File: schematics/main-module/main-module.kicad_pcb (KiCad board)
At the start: 4 copper layers, 134 x 52 mm, 101 parts, among them J1 Conn_01x02_Socket, J2 USB_C_Receptacle_USB2.0, J3 Charger, J4 Power, J5 Limit Switch, J6 Conn_01x04_Socket, Q1 IRLML0030, Q2 IRF7425PbF, Q3 BC847, Q4 BC847, Q6 IRLML0030, Q7 IRF7832PbF, Q8 IRF7832PbF, SW1 KLS7-TS3601-5.0-180, SW2 KLS7-TS3601-5.0-180, T1 Transformer_1P_SS, U1 CP2102N-Axx-xQFN28, U10 SRX882@315Mhz, U11 FAN3100, U12 FAN3100, U13 TMC2209_Module, U3 AMS1117-5.0, U4 AMS1117-3.3, U6 SRX882@433Mhz, U7 STX882@433Mhz, U8 ESP32-WROOM-32, U9 TL494

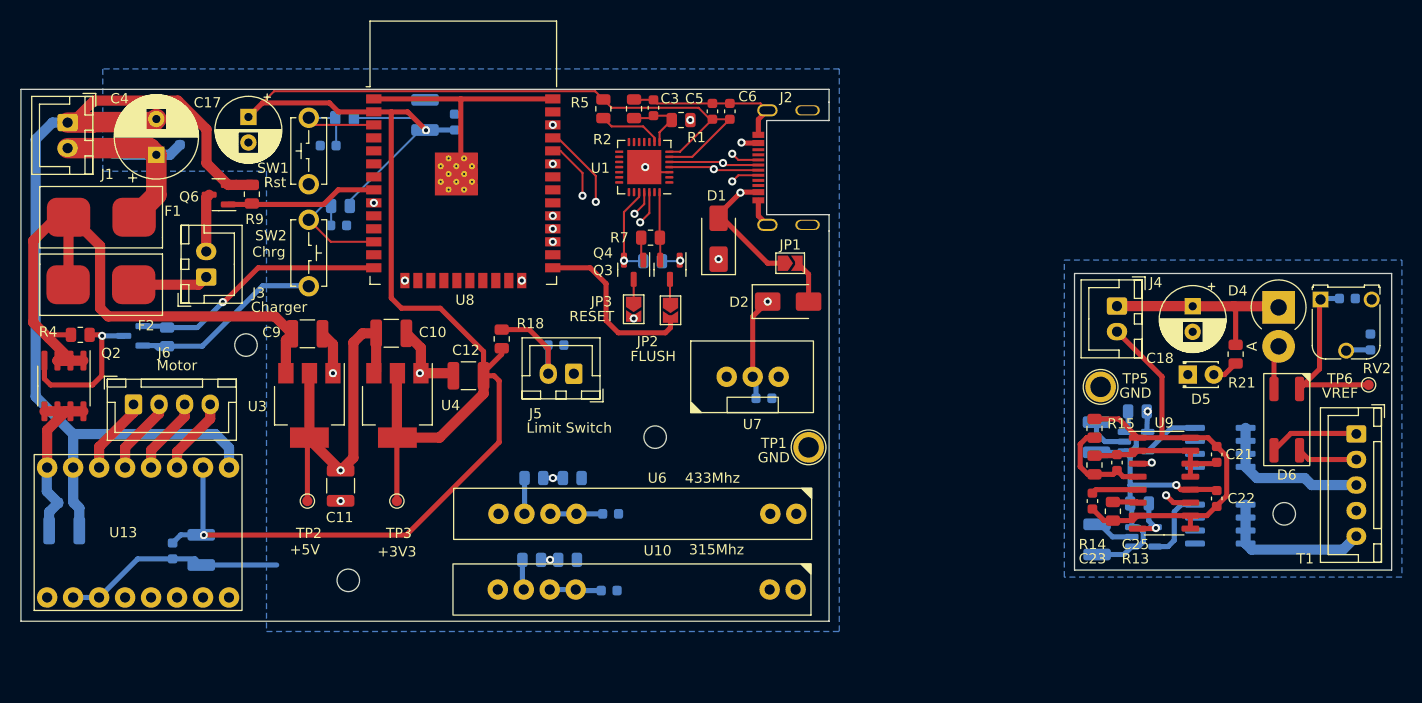
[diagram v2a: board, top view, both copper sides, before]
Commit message: 1. board: added protection against high noise in case of endstop is broken. 2. board: added step-up 7.5V -> 15V for charger. 3. firmware - added support for noise protection and some changes in stepper logic
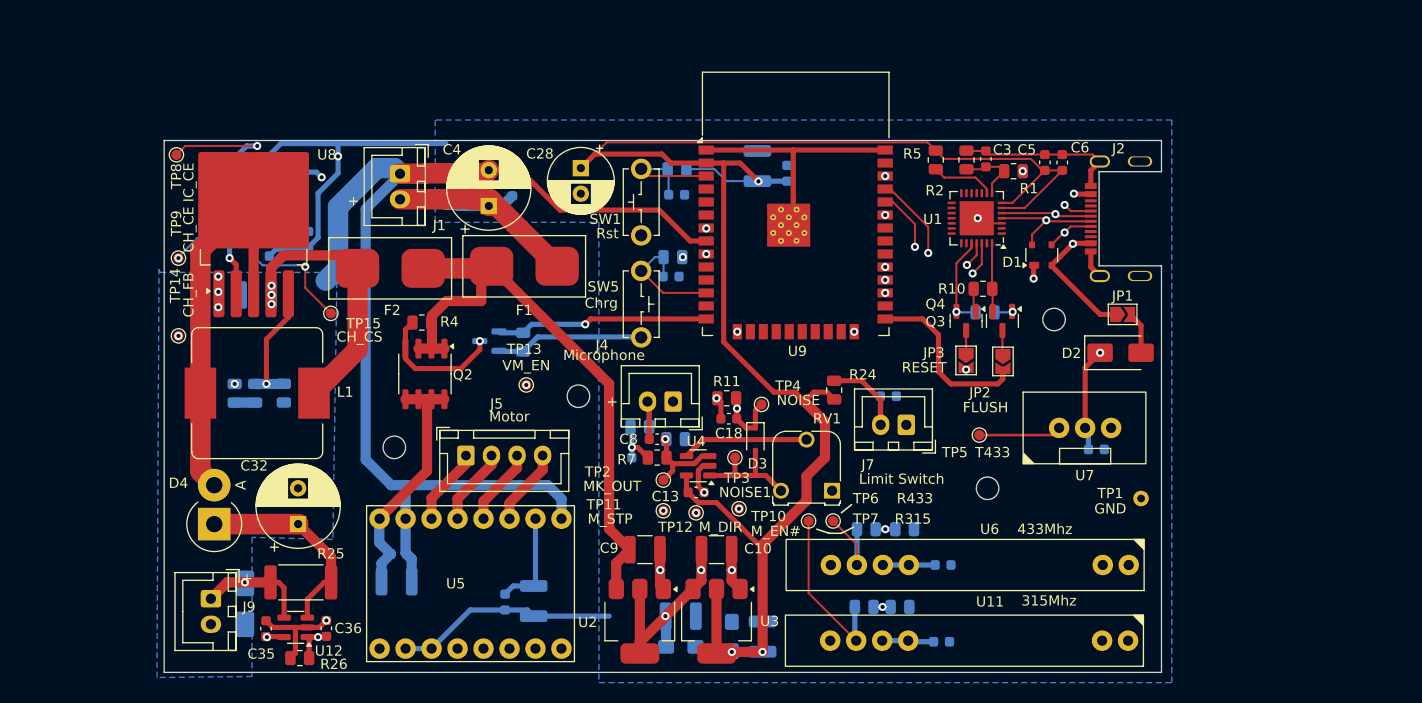
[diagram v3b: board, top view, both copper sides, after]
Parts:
- removed the C21 at (158.9, 77.7)
- removed the C22 at (158.9, 82.0)
- removed the C23 at (146.8, 82.2)
- removed the C28 at (147.2, 76.0)
- removed the C30 at (147.2, 86.0)
- removed the H3 at (74.0, 90.0)
- removed J3: Charger, Connector_JST:JST_XH_B2B-XH-A_1x02_P2.50mm_Vertical
- removed Q6: IRLML0030, Package_TO_SOT_SMD:SOT-23
- removed Q7, Q8: IRF7832PbF, Package_SO:SOIC-8_3.9x4.9mm_P1.27mm
- removed the R13 at (148.8, 83.2)
- removed the R14 at (146.9, 78.7)
- removed the R9 at (64.6, 52.2)
- removed RV2: 1K, Potentiometer_THT:Potentiometer_Runtron_RM-065_Vertical
- removed T1: Transformer_1P_SS, Connector_JST:JST_XH_B5B-XH-A_1x05_P2.50mm_Vertical
- removed the U11 at (151.7, 85.8)
- removed the U9 at (153.8, 80.5)
- added C13: 100 nF, Capacitor_SMD:C_0603_1608Metric, F.Cu at (108.0, 81.4)
- added C16: 22 uF, Capacitor_Tantalum_SMD:CP_EIA-3216-10_Kemet-I_Pad1.58x1.35mm_HandSolder, B.Cu at (106.5, 96.5)
- added C17: 22 uF, Capacitor_Tantalum_SMD:CP_EIA-3216-10_Kemet-I_Pad1.58x1.35mm_HandSolder, B.Cu at (111.5, 95.5)
- added C24: 22 uF, Capacitor_SMD:C_1210_3225Metric, B.Cu at (65.0, 62.1)
- added C26: 10 nF, Capacitor_SMD:C_0603_1608Metric, B.Cu at (70.1, 56.7)
- added C29: 100 nF, Capacitor_SMD:C_0603_1608Metric, B.Cu at (65.4, 50.1)
- added C32: 220 uF@35V, Capacitor_THT:CP_Radial_D8.0mm_P3.50mm, F.Cu at (69.1, 84.5)
- added C36: 10 nF, Capacitor_SMD:C_0603_1608Metric, F.Cu at (71.9, 94.7)
- added C7: 100 nF, Capacitor_SMD:C_0603_1608Metric, B.Cu at (102.5, 78.0)
- added C8: 47 nF, Capacitor_SMD:C_0603_1608Metric, F.Cu at (104.2, 76.2)
- added D3: BAV21WS, Diode_SMD:D_SOD-323F, F.Cu at (113.8, 76.2)
- added H4: MountingHole, MountingHole:MountingHole_2.2mm_M2, F.Cu at (143.0, 64.5)
- added J9: Charger port, Connector_JST:JST_XH_B2B-XH-A_1x02_P2.50mm_Vertical, F.Cu at (60.6, 91.8)
- added L1: AMPLF1260, 4.7 uH, Inductor_SMD:L_TaiTech_TMPC1265_13.5x12.5mm, F.Cu at (65.1, 71.7)
- added R11: 10K, Resistor_SMD:R_0805_2012Metric, F.Cu at (111.0, 72.2)
- added R18: 200K, Resistor_SMD:R_0805_2012Metric, B.Cu at (60.2, 55.6)
- added R19: 1K, Resistor_SMD:R_0805_2012Metric, B.Cu at (62.9, 71.7)
- added R20: 10K, Resistor_SMD:R_0805_2012Metric, B.Cu at (64.9, 71.7)
- added R25: 0,5, Resistor_SMD:R_2512_6332Metric, F.Cu at (69.4, 90.2)
- added R26: 100K, Resistor_SMD:R_0805_2012Metric, F.Cu at (69.3, 97.6)
- added R6: 10K, Resistor_SMD:R_0805_2012Metric, B.Cu at (102.5, 75.0)
- added R7: 20K, Resistor_SMD:R_0805_2012Metric, F.Cu at (104.2, 78.0)
- added R8: 10K, Resistor_SMD:R_0805_2012Metric, B.Cu at (106.0, 76.2)
- added RV1: RM065, 100K, Potentiometer_THT:Potentiometer_Runtron_RM-065_Vertical, F.Cu at (121.3, 81.2)
- added TP10: M_EN#, TestPoint:TestPoint_Pad_D1.0mm, F.Cu at (112.2, 83.0)
- added TP11: M_STP, TestPoint:TestPoint_Pad_D1.0mm, F.Cu at (104.8, 83.2)
- added TP12: M_DIR, TestPoint:TestPoint_Pad_D1.0mm, F.Cu at (108.0, 83.4)
- added TP13: VM_EN, TestPoint:TestPoint_Pad_D1.0mm, F.Cu at (91.4, 70.9)
- added TP14: CH_FB, TestPoint:TestPoint_Pad_D1.0mm, F.Cu at (57.4, 66.1)
- added TP15: CH_CS, TestPoint:TestPoint_Pad_D1.0mm, F.Cu at (72.3, 63.9)
- added TP4: NOISE, TestPoint:TestPoint_Pad_D1.0mm, F.Cu at (114.4, 72.8)
- added TP7: R315, TestPoint:TestPoint_Pad_D1.0mm, F.Cu at (119.0, 84.2)
- added TP8: IC_CE, TestPoint:TestPoint_Pad_D1.0mm, F.Cu at (57.2, 48.4)
- added TP9: CH_CE, TestPoint:TestPoint_Pad_D1.0mm, F.Cu at (57.4, 58.5)
- added U10: TL331, Package_TO_SOT_SMD:SOT-23-5, B.Cu at (65.2, 53.1)
- added U4: AD8541, Package_TO_SOT_SMD:SOT-23-5, F.Cu at (108.2, 78.8)
- added U8: XL6009, Package_TO_SOT_SMD:TO-263-5_TabPin3, F.Cu at (64.7, 54.3)
- C14: renamed from C11; moved to B.Cu
- C15: renamed from C12; moved to B.Cu
- C18: value 100 uF -> 1 uF; footprint Capacitor_THT:CP_Radial_D6.3mm_P2.50mm -> Capacitor_SMD:C_0603_1608Metric
- C25: value 500 nF -> 10 nF; moved to B.Cu
- C35: moved to F.Cu
- D1: value SMAJ5.0CA-TR -> SP0503BAHT; footprint Diode_SMD:D_SMA -> Package_TO_SOT_SMD:SOT-143
- D4: value HER508 -> SR540
- D5: value LED -> BAV21WS; footprint LED_THT:LED_D1.8mm_W3.3mm_H2.4mm -> Diode_SMD:D_SOD-323F; moved to B.Cu
- D6: value MB10S -> SMAJ26A; footprint Library:MBS -> Diode_SMD:D_SMA; moved to B.Cu
- J4: value Power -> Microphone
- R15: value 1K -> 10K; moved to B.Cu
- R16: value 1K -> 200
- R17: value 1K -> 620
- R21: moved to B.Cu
- TP1: footprint TestPoint:TestPoint_Plated_Hole_D2.0mm -> Library:TestPoint_Plated_Hole_D1.0mm
- TP2: value +5V -> MK_OUT
- TP3: value +3V3 -> NOISE1
- TP5: value GND -> T433; footprint TestPoint:TestPoint_Plated_Hole_D2.0mm -> TestPoint:TestPoint_Pad_D1.0mm
- TP6: value VREF -> R433
- U12: value FAN3100 -> INA169; moved to F.Cu
- moved C35 111.5 mm to (66.0, 94.7)
- moved C33 106.7 mm to (65.2, 56.3), turned to 180 degrees
- moved D4 106.2 mm to (60.9, 84.5), turned to 90 degrees
- moved D6 103.4 mm to (63.9, 92.3)
- moved D5 94.8 mm to (62.4, 55.6), turned to 90 degrees
- moved R21 93.1 mm to (67.7, 71.7), turned to 90 degrees
- moved R17 91.4 mm to (62.4, 51.8), turned to 90 degrees
- moved H1 87.2 mm to (78.5, 77.0)
- moved R16 87.1 mm to (68.2, 56.7), turned to 90 degrees
- moved C25 86.1 mm to (65.5, 58.3), turned to 180 degrees
- moved U12 84.1 mm to (68.9, 94.6), turned to 180 degrees
- moved R15 81.8 mm to (68.2, 53.0)
- moved TP6 54.0 mm to (121.4, 84.2)
- moved C18 46.7 mm to (111.2, 74.2), turned to 180 degrees
- moved J4 44.4 mm to (105.8, 72.5), turned to 180 degrees
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- renumbered C27 to C11, C29 to C12, C31 to C19, C14 to C20, C15 to C21, C32 to C22, C16 to C23, C24 to C27, C17 to C28, C19 to C30, C20 to C31, C26 to C34, C34 to C37, H4 to H3, J6 to J5, J5 to J7, R7 to R10, R10 to R12, R11 to R13, R12 to R14, R19 to R22, R20 to R23, R18 to R24, R22 to R29, R6 to R9, SW2 to SW5, U10 to U11, U3 to U2, U4 to U3, U13 to U5, U8 to U9
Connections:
- C18 pad 1: VPP -> /NOISE
- C18 pad 2: GND1 -> GNDA
- C25 pad 1: /TL494_VREF -> GNDA
- C25 pad 2: /TL494_DTC -> /CHARGER_CURRENT_SENCE
- C33 pad 1: Net-(D6-+) -> GNDA
- C33 pad 2: GND1 -> /CHARGER_ENABLE
- C35 pad 1: /TL494_FEEDBACK -> +5V
- C35 pad 2: GND1 -> GNDA
- D4 pad 1: VPP -> Net-(D4-K)
- D4 pad 2: GND1 -> Net-(D4-A)
- D5 pad 1: GND1 -> /CHARGER_ENABLE
- D6 pad 1: Net-(D6-+) -> Net-(D6-A1)
- D6 pad 2: GND1 -> GNDPWR
- F2 pad 2: Net-(J3-Pin_1) -> /+7.5V_CHARGER_AFTER_FUSE
- J4 pad 1: VPP -> GNDA
- J4 pad 2: GND1 -> Net-(J4-Pin_2)
- R15 pad 1: /TL494_DTC -> Net-(U10--)
- R15 pad 2: GND1 -> +5V
- R16 pad 1: VPP -> GNDA
- R16 pad 2: Net-(U11-IN-) -> Net-(U10--)
- R17 pad 1: VPP -> Net-(D5-A)
- R17 pad 2: Net-(U12-IN-) -> /IC_CHARGER_ENABLE
- R21 pad 1: VPP -> GNDPWR
- R21 pad 2: Net-(D5-A) -> /CHARGER_FEEDBACK
- TP2 pad 1: +5V -> Net-(U4-Vin+)
- TP3 pad 1: +3V3 -> Net-(D3-A)
- TP5 pad 1: GND1 -> /FM_OUT_433
- TP6 pad 1: Net-(D6-+) -> /FM_IN_5V_433
- U12 pad 1: VPP -> /CHARGER_CURRENT_SENCE
- U12 pad 2: GND1 -> GNDA
- U12 pad 3: VPP -> Net-(D4-K)
- U12 pad 4: Net-(U12-IN-) -> Net-(D6-A1)
- U12 pad 5: Net-(Q8-G) -> +5V
- U9 pad 7: unconnected-(U8-IO35-Pad7) -> /NOISE
- U9 pad 8: /CHARGER_ENABLE -> /IC_CHARGER_ENABLE
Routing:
- net +5V: track 122.4 -> 240.5 mm, vias 2 -> 6
- net GNDA: track 101.1 -> 200.1 mm, vias 6 -> 9
- net VPP: track 93.8 -> 0.00 mm, vias 1 -> 0
- net /IC_CHARGER_ENABLE: track 0.00 -> 61.0 mm, vias 0 -> 2
- net GND1: track 57.8 -> 0.00 mm
- net /CHARGER_CURRENT_SENCE: track 0.00 -> 56.4 mm, vias 0 -> 2
- net Net-(D4-K): track 0.00 -> 36.3 mm, vias 0 -> 1
- net Net-(D4-A): track 0.00 -> 36.1 mm
- net /TL494_FEEDBACK: track 27.3 -> 0.00 mm, vias 1 -> 0
- net /NOISE: track 0.00 -> 26.7 mm, vias 0 -> 2
- net /CHARGER_FEEDBACK: track 0.00 -> 24.4 mm, vias 0 -> 2
- net /+7.5V_CHARGER_AFTER_FUSE: track 0.00 -> 24.2 mm, vias 0 -> 3
- net Net-(D6-+): track 18.1 -> 0.00 mm
- net Net-(T1-SB): track 15.4 -> 0.00 mm
- net Net-(T1-SA): track 15.4 -> 0.00 mm
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- added copper zone on B.Cu, net GNDPWR
- removed copper zone on B.Cu, net GND1
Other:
- board size 134 x 52 mm -> 97.5 x 52 mm
- board text added: "0,0000 mm / 0,0000 mm"
- board text added: "0,2000 mm"
- board text added: "1,6000 mm"
- board text added: "4"
- board text added: "97,5000 mm x 52,0000 mm"
- board text added: "ACW-main-v1.3"
- board text added: "None"
- board text added: "Габариты платы:"
- board text added: "Количество слоёв меди:"
- board text added: "Контроль импеданса:"
- board text added: "Краевой соединитель:"
- board text added: "Метал. торцы:"
- board text added: "Мин. дорожка/зазор:"
- board text added: "Мин. сверло:"
- board text added: "Нет"
- board text added: "Периферийные полу-отверстия:"
- board text added: "Покрытие меди:"
- board text added: "Толщина платы:"
- board text added: "ХАРАКТЕРИСТИКИ ПЛАТЫ"
- board text removed: "ACW-charger-v1.0"
- board text removed: "ACW-main-v1.0"
